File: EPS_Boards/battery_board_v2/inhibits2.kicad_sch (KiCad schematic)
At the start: 6 parts, among them Q11 NTJD1155LT1G, U13 TPS24750

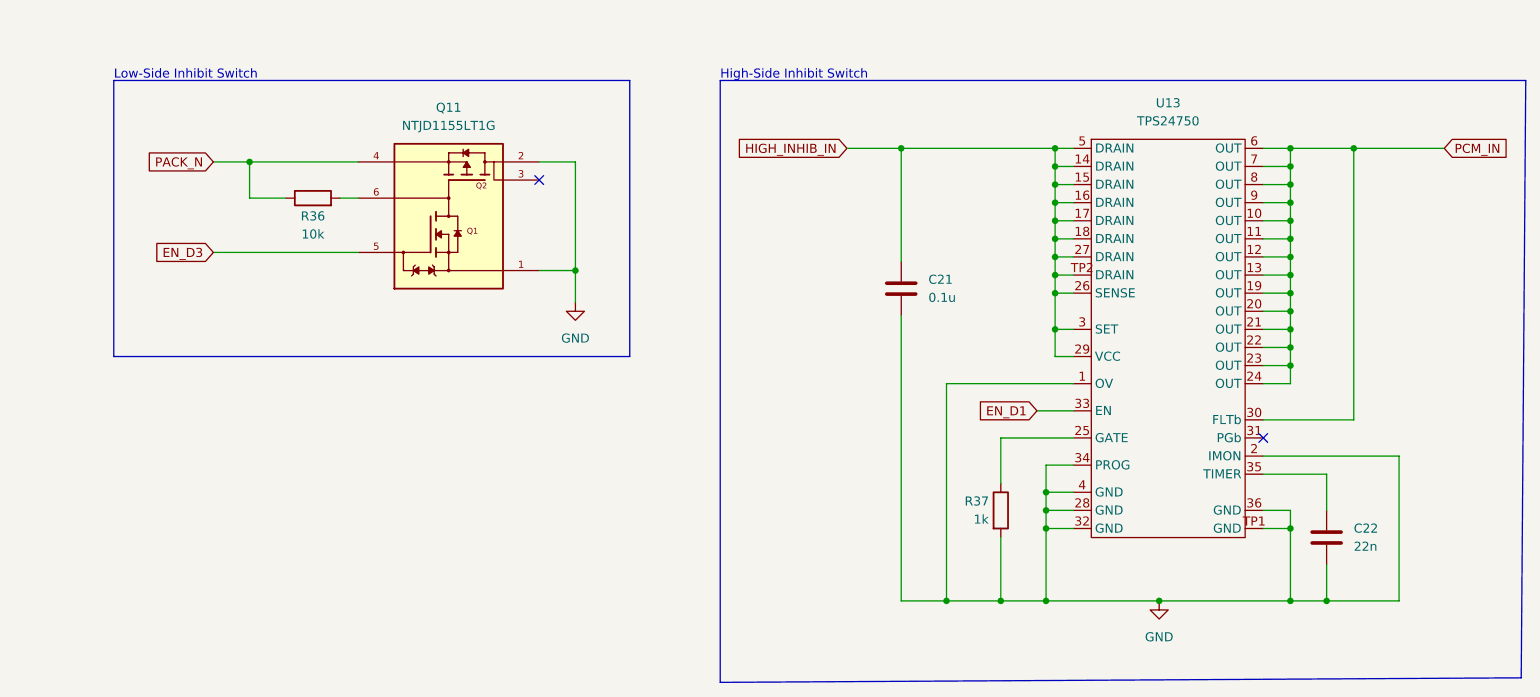
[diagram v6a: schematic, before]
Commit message: eps: battery board: more design review changes
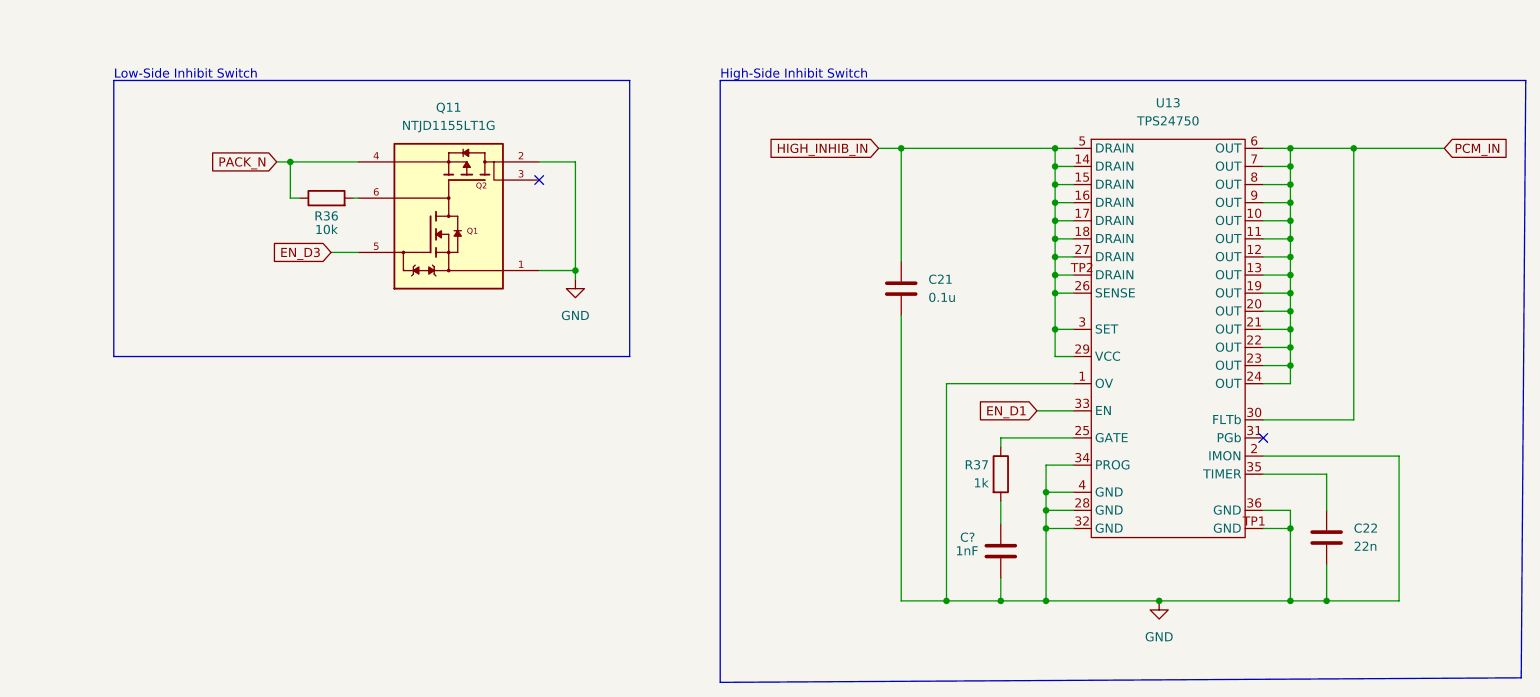
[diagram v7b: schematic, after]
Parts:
- added C?: 1nF, symbol Device:C
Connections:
- net GND: now also C?.2; no longer R37.2
- new net: C?.1, R37.2
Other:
- moved on the sheet: R36, R37

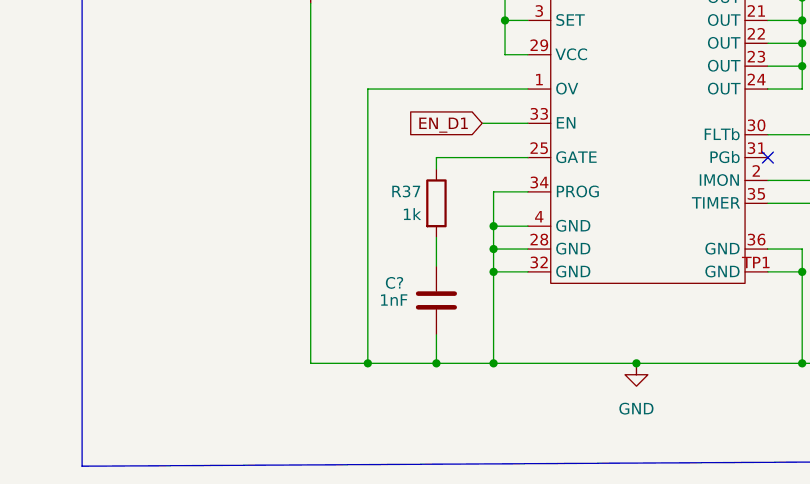
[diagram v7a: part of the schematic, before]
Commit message: eps: battery board: design review schematic changes
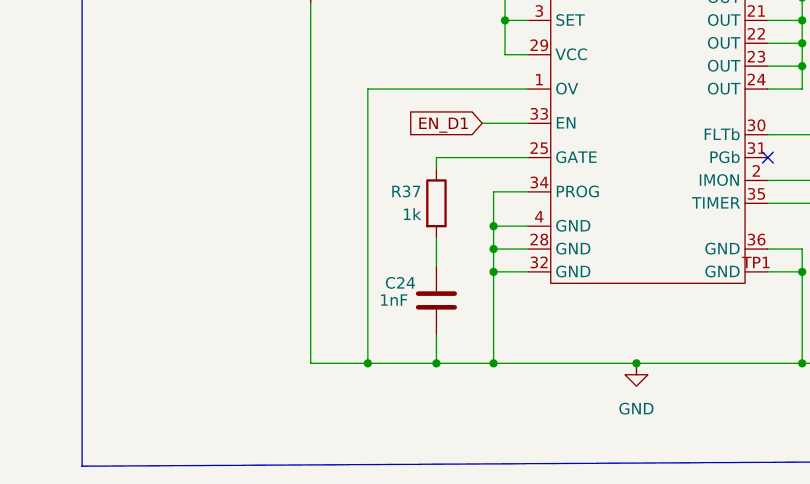
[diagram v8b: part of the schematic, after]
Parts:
- C24: renamed from C?; footprint (none) -> Capacitor_SMD:C_01005_0402Metric
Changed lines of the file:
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@@
   (symbol (lib_id "Device:C") (at 175.26 100.965 0) (unit 1)
     (in_bom yes) (on_board yes)
-    (property "Reference" "C?" (id 0) (at 169.545 99.06 0)
+    (property "Reference" "C24" (id 0) (at 169.545 99.06 0)
       (effects (font (size 1.27 1.27)) (justify left))
     )
@@
       (effects (font (size 1.27 1.27)) (justify left))
     )
-    (property "Footprint" "" (id 2) (at 176.2252 104.775 0)
+    (property "Footprint" "Capacitor_SMD:C_01005_0402Metric" (id 2) (at 176.2252 104.775 0)
       (effects (font (size 1.27 1.27)) hide)
     )
